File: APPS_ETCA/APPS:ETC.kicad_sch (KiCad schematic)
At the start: 7 parts, among them U1 NUCLEO-L432KC, U2 ISO1050DUB, U3 A1365xKTTN-1, U4 A1365xKTTN-1, U5 L78S05CV

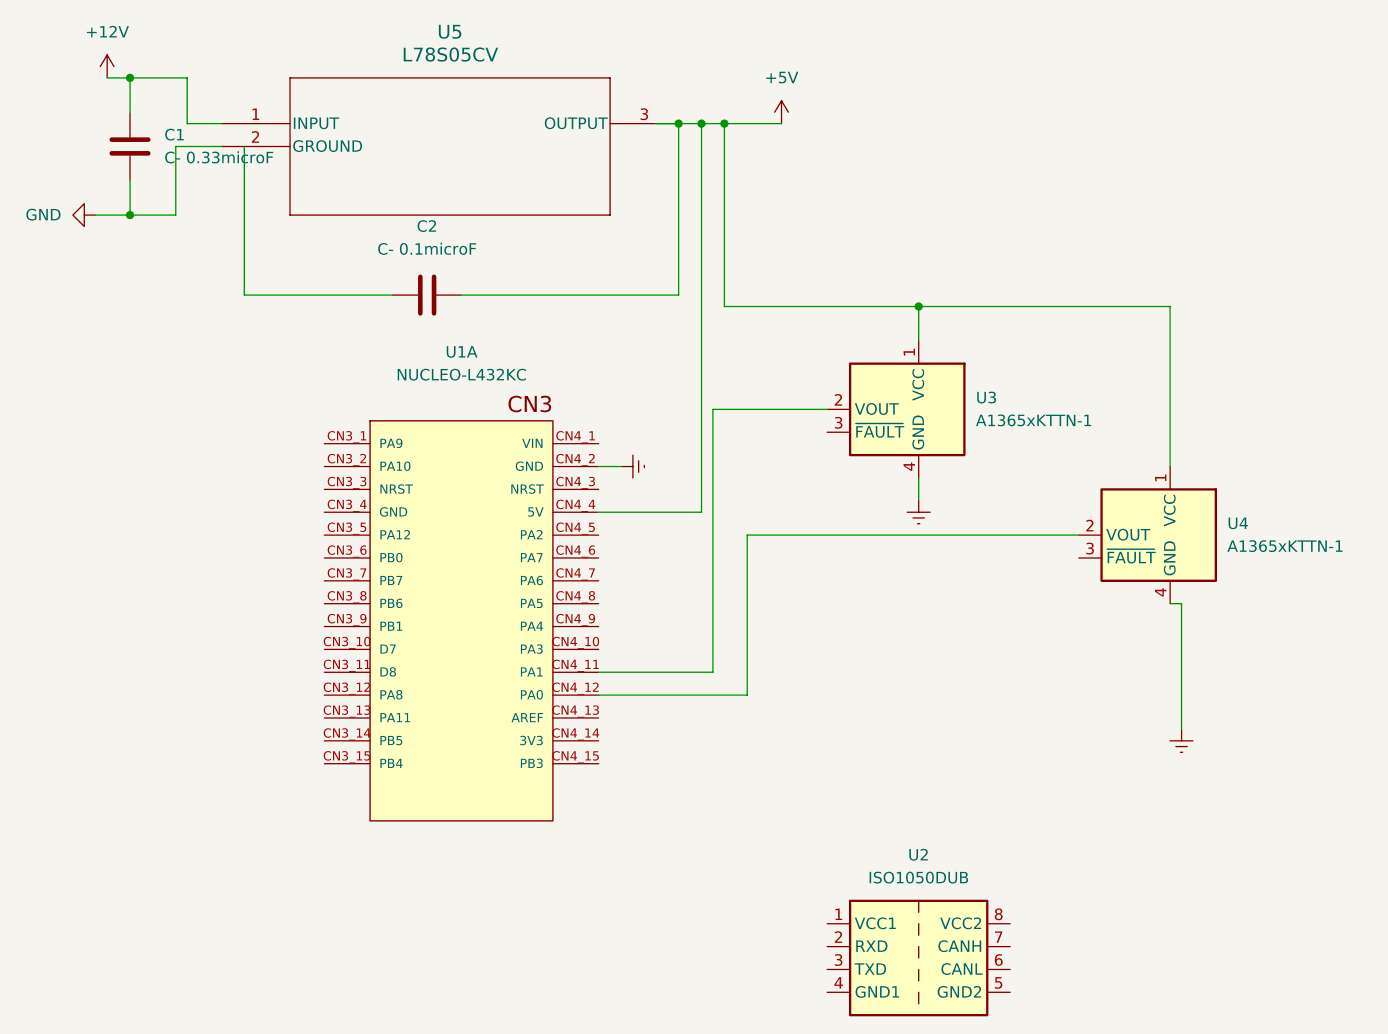
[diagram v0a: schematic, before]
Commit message: updating apps/etc schema
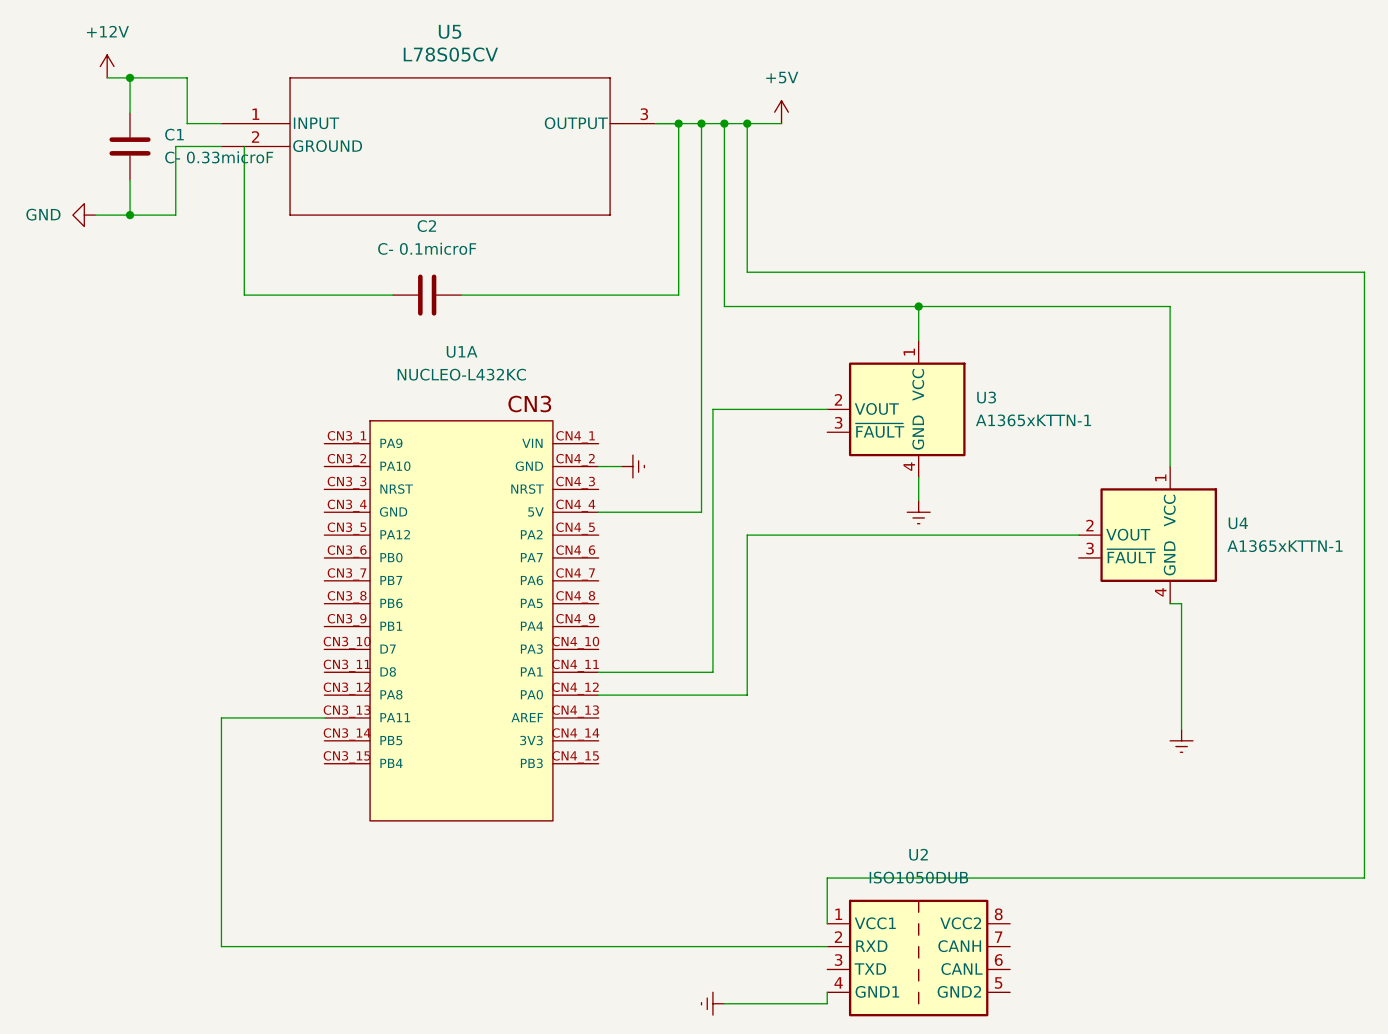
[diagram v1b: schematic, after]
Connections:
- net +5V: now also U2.1 (VCC1)
- net Earth: now also U2.4 (GND1)
- net at U1.CN3_13 (PA11): now also U2.2 (RXD)
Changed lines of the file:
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@@
   (junction (at 76.2 24.13) (diameter 0) (color 0 0 0 0)
+  )
+  (junction (at 144.78 29.21) (diameter 0) (color 0 0 0 0)
   )
   (wire (pts (xy 163.83 49.53) (xy 191.77 49.53))
@@
     (stroke (width 0) (type default))
   )
+  (wire (pts (xy 213.36 113.03) (xy 153.67 113.03))
+    (stroke (width 0) (type default))
+  )
   (wire (pts (xy 163.83 68.58) (xy 163.83 71.12))
     (stroke (width 0) (type default))
   )
   (wire (pts (xy 128.27 67.31) (xy 130.81 67.31))
+    (stroke (width 0) (type default))
+  )
+  (wire (pts (xy 86.36 120.65) (xy 153.67 120.65))
+    (stroke (width 0) (type default))
+  )
+  (wire (pts (xy 142.24 127) (xy 153.67 127))
     (stroke (width 0) (type default))
   )
@@
     (stroke (width 0) (type default))
   )
+  (wire (pts (xy 153.67 113.03) (xy 153.67 118.11))
+    (stroke (width 0) (type default))
+  )
   (wire (pts (xy 76.2 35.56) (xy 76.2 39.37))
     (stroke (width 0) (type default))
   )
   (wire (pts (xy 134.62 29.21) (xy 137.16 29.21))
+    (stroke (width 0) (type default))
+  )
+  (wire (pts (xy 97.79 95.25) (xy 86.36 95.25))
     (stroke (width 0) (type default))
   )
@@
   )
   (wire (pts (xy 137.16 48.26) (xy 137.16 29.21))
+    (stroke (width 0) (type default))
+  )
+  (wire (pts (xy 86.36 95.25) (xy 86.36 120.65))
     (stroke (width 0) (type default))
   )
@@
     (stroke (width 0) (type default))
   )
+  (wire (pts (xy 213.36 45.72) (xy 213.36 113.03))
+    (stroke (width 0) (type default))
+  )
+  (wire (pts (xy 153.67 127) (xy 153.67 125.73))
+    (stroke (width 0) (type default))
+  )
   (wire (pts (xy 81.28 39.37) (xy 81.28 31.75))
     (stroke (width 0) (type default))
@@
   )
   (wire (pts (xy 76.2 39.37) (xy 81.28 39.37))
+    (stroke (width 0) (type default))
+  )
+  (wire (pts (xy 144.78 29.21) (xy 142.24 29.21))
     (stroke (width 0) (type default))
   )
@@
     (stroke (width 0) (type default))
   )
+  (wire (pts (xy 144.78 45.72) (xy 213.36 45.72))
+    (stroke (width 0) (type default))
+  )
   (wire (pts (xy 82.55 24.13) (xy 82.55 29.21))
     (stroke (width 0) (type default))
@@
     (stroke (width 0) (type default))
   )
+  (wire (pts (xy 144.78 29.21) (xy 144.78 45.72))
+    (stroke (width 0) (type default))
+  )
   (wire (pts (xy 142.24 29.21) (xy 142.24 49.53))
     (stroke (width 0) (type default))
@@
     (stroke (width 0) (type default))
   )
-  (wire (pts (xy 148.59 29.21) (xy 142.24 29.21))
+  (wire (pts (xy 148.59 29.21) (xy 144.78 29.21))
     (stroke (width 0) (type default))
   )
@@
         )
       )
+    )
+  )
+  (symbol (lib_id "power:Earth") (at 142.24 127 270) (unit 1)
+    (in_bom yes) (on_board yes) (dnp no) (fields_autoplaced)
+    (property "Reference" "#PWR07" (at 135.89 127 0)
+      (effects (font (size 1.27 1.27)) hide)
+    )
+    (property "Value" "Earth" (at 138.43 127 0)
+      (effects (font (size 1.27 1.27)) hide)
+    )
+    (property "Footprint" "" (at 142.24 127 0)
+      (effects (font (size 1.27 1.27)) hide)
+    )
+    (property "Datasheet" "~" (at 142.24 127 0)
+      (effects (font (size 1.27 1.27)) hide)
+    )
+    (pin "1")
+    (instances
+      (project "APPS:ETC"
+        (path "/21da8b0a-bf7f-4003-9579-5de7190091be"
+          (reference "#PWR07") (unit 1)
+        )
+      )
